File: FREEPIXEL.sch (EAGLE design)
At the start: 4 parts

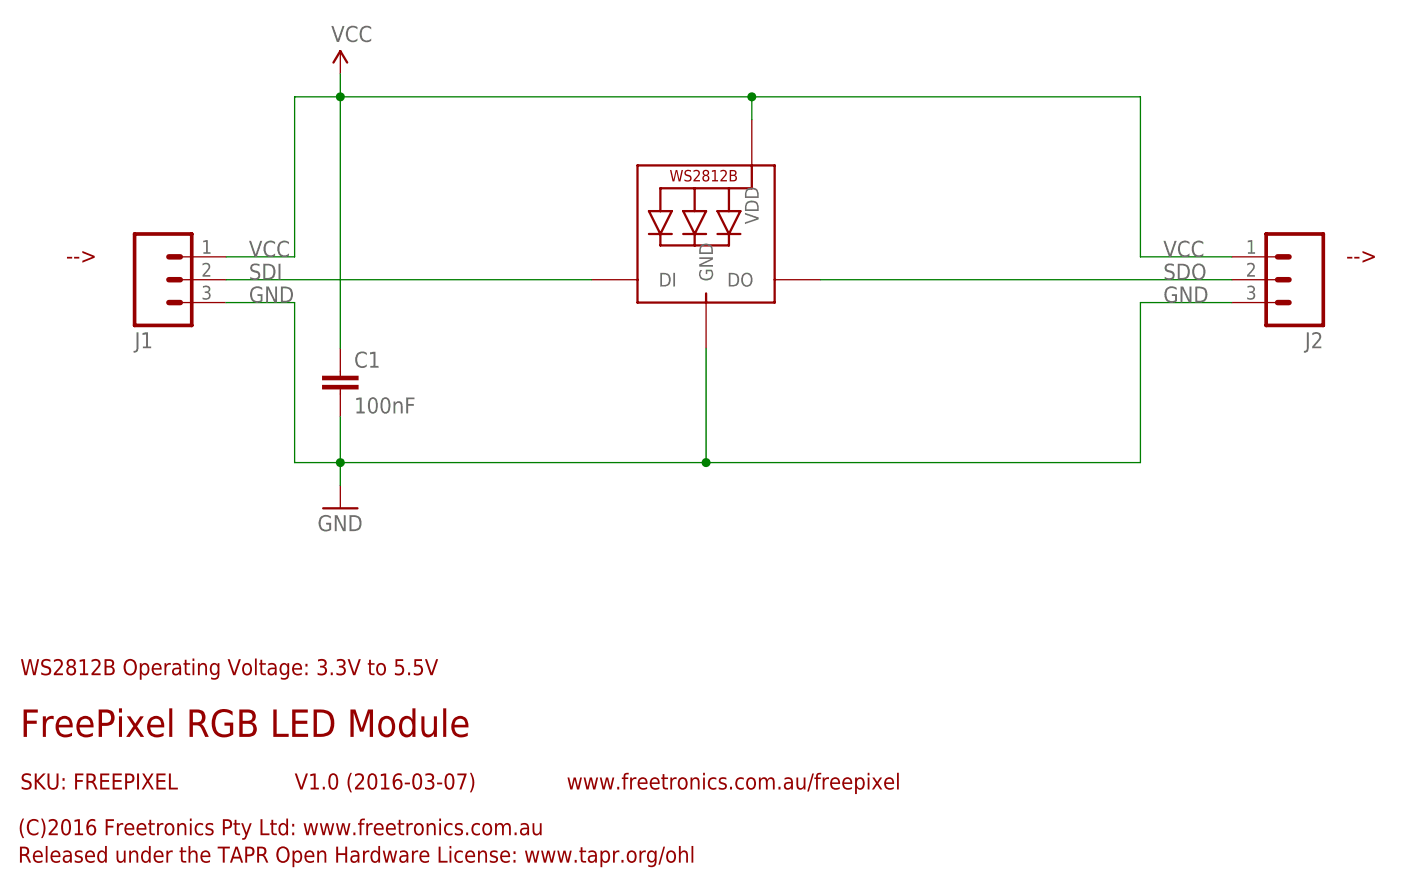
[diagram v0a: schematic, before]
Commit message: Clarified schematic
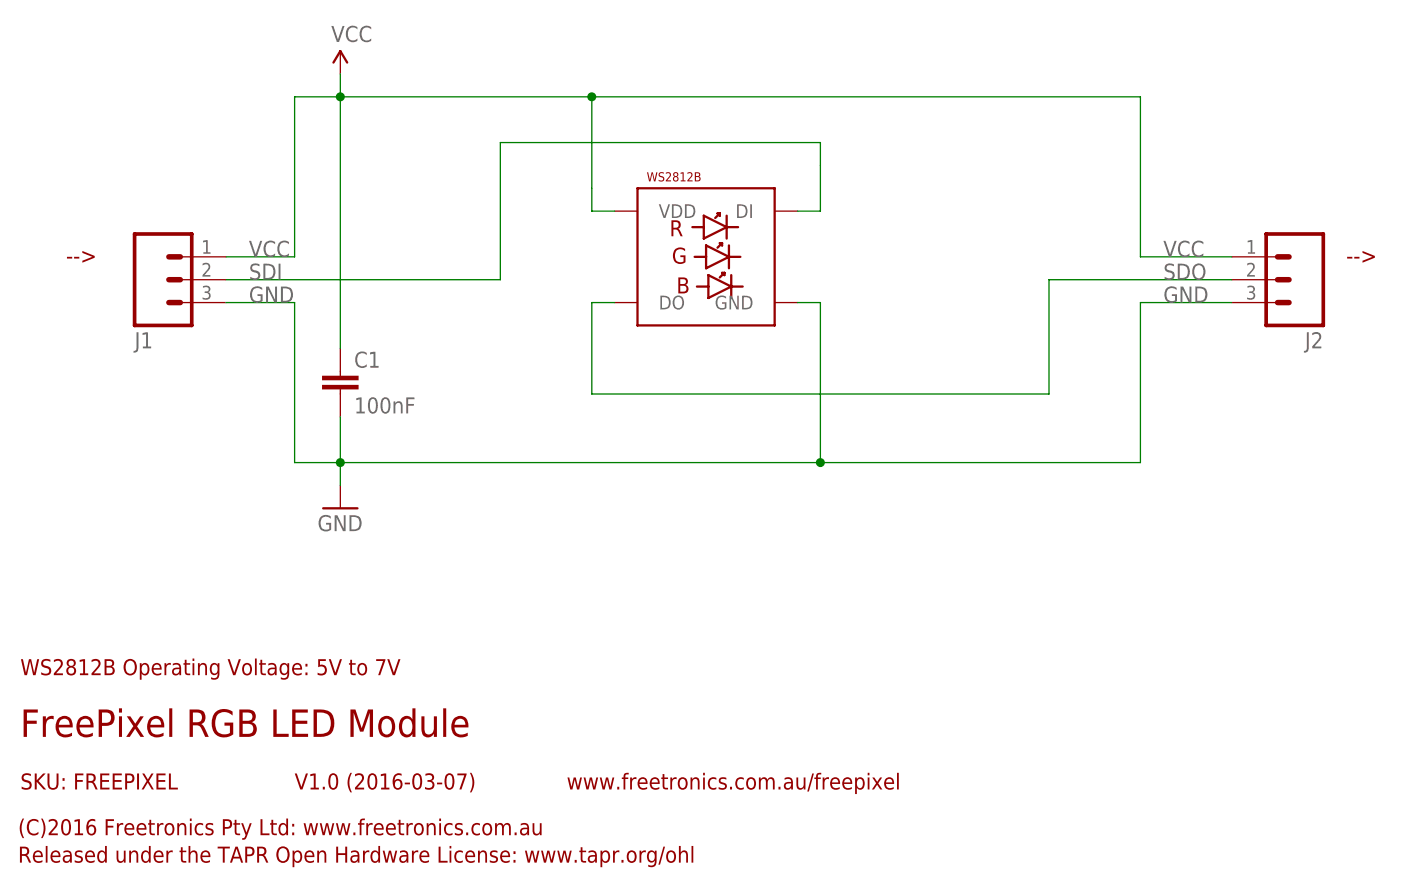
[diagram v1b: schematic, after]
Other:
- note added: "WS2812B Operating Voltage: 5V to 7V"
- note removed: "WS2812B Operating Voltage: 3.3V to 5.5V"
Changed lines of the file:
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@@
 <text x="7.366" y="6.35" size="1.778" layer="94">Released under the TAPR Open Hardware License: www.tapr.org/ohl</text>
 <text x="68.326" y="14.478" size="1.778" layer="94">www.freetronics.com.au/freepixel</text>
-<text x="7.62" y="27.178" size="1.778" layer="94">WS2812B Operating Voltage: 3.3V to 5.5V</text>
+<text x="7.62" y="27.178" size="1.778" layer="94">WS2812B Operating Voltage: 5V to 7V</text>
 <text x="12.7" y="72.898" size="1.778" layer="94">--&gt;</text>
 <text x="154.94" y="72.898" size="1.778" layer="94">--&gt;</text>
@@
 <pinref part="GND5" gate="1" pin="GND"/>
 <pinref part="J1" gate="G$1" pin="3"/>
-<wire x1="43.18" y1="50.8" x2="83.82" y2="50.8" width="0.1524" layer="91"/>
-<wire x1="83.82" y1="50.8" x2="132.08" y2="50.8" width="0.1524" layer="91"/>
+<wire x1="43.18" y1="50.8" x2="96.52" y2="50.8" width="0.1524" layer="91"/>
+<wire x1="96.52" y1="50.8" x2="132.08" y2="50.8" width="0.1524" layer="91"/>
 <wire x1="142.24" y1="68.58" x2="132.08" y2="68.58" width="0.1524" layer="91"/>
 <wire x1="132.08" y1="68.58" x2="132.08" y2="50.8" width="0.1524" layer="91"/>
@@
 <pinref part="J2" gate="G$1" pin="3"/>
 <pinref part="LED1" gate="G$1" pin="GND"/>
-<wire x1="83.82" y1="63.5" x2="83.82" y2="50.8" width="0.1524" layer="91"/>
-<junction x="83.82" y="50.8"/>
+<wire x1="93.98" y1="68.58" x2="96.52" y2="68.58" width="0.1524" layer="91"/>
+<wire x1="96.52" y1="68.58" x2="96.52" y2="50.8" width="0.1524" layer="91"/>
+<junction x="96.52" y="50.8"/>
 </segment>
 </net>
 <net name="SDI" class="0">
 <segment>
-<wire x1="30.48" y1="71.12" x2="71.12" y2="71.12" width="0.1524" layer="91"/>
+<wire x1="30.48" y1="71.12" x2="60.96" y2="71.12" width="0.1524" layer="91"/>
+<wire x1="60.96" y1="71.12" x2="60.96" y2="86.36" width="0.1524" layer="91"/>
+<wire x1="60.96" y1="86.36" x2="96.52" y2="86.36" width="0.1524" layer="91"/>
+<wire x1="96.52" y1="86.36" x2="96.52" y2="83.82" width="0.1524" layer="91"/>
+<wire x1="96.52" y1="83.82" x2="96.52" y2="78.74" width="0.1524" layer="91"/>
+<wire x1="96.52" y1="78.74" x2="93.98" y2="78.74" width="0.1524" layer="91"/>
 <label x="33.02" y="71.12" size="1.778" layer="95"/>
 <pinref part="LED1" gate="G$1" pin="DI"/>
@@
 <net name="SDO" class="0">
 <segment>
-<wire x1="96.52" y1="71.12" x2="142.24" y2="71.12" width="0.1524" layer="91"/>
+<wire x1="73.66" y1="68.58" x2="71.12" y2="68.58" width="0.1524" layer="91"/>
+<wire x1="71.12" y1="68.58" x2="71.12" y2="58.42" width="0.1524" layer="91"/>
+<wire x1="71.12" y1="58.42" x2="121.92" y2="58.42" width="0.1524" layer="91"/>
+<wire x1="121.92" y1="58.42" x2="121.92" y2="71.12" width="0.1524" layer="91"/>
+<wire x1="121.92" y1="71.12" x2="142.24" y2="71.12" width="0.1524" layer="91"/>
 <label x="134.62" y="71.12" size="1.778" layer="95"/>
 <pinref part="LED1" gate="G$1" pin="DO"/>
@@
 <label x="134.62" y="73.66" size="1.778" layer="95"/>
 <pinref part="J2" gate="G$1" pin="1"/>
-<wire x1="43.18" y1="91.44" x2="88.9" y2="91.44" width="0.1524" layer="91"/>
+<wire x1="43.18" y1="91.44" x2="71.12" y2="91.44" width="0.1524" layer="91"/>
 <pinref part="LED1" gate="G$1" pin="VDD"/>
-<wire x1="88.9" y1="91.44" x2="132.08" y2="91.44" width="0.1524" layer="91"/>
-<wire x1="88.9" y1="91.44" x2="88.9" y2="88.9" width="0.1524" layer="91"/>
-<junction x="88.9" y="91.44"/>
+<wire x1="71.12" y1="91.44" x2="132.08" y2="91.44" width="0.1524" layer="91"/>
+<wire x1="71.12" y1="91.44" x2="71.12" y2="81.28" width="0.1524" layer="91"/>
+<wire x1="71.12" y1="81.28" x2="71.12" y2="78.74" width="0.1524" layer="91"/>
+<wire x1="71.12" y1="78.74" x2="73.66" y2="78.74" width="0.1524" layer="91"/>
+<junction x="71.12" y="91.44"/>
 </segment>
 </net>

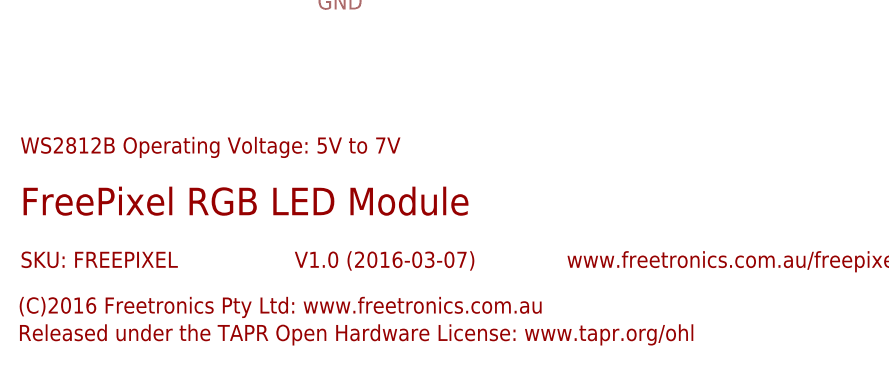
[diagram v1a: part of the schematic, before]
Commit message: Fixed silkscreen label for DI (Data In) on bottom for v1.1 release
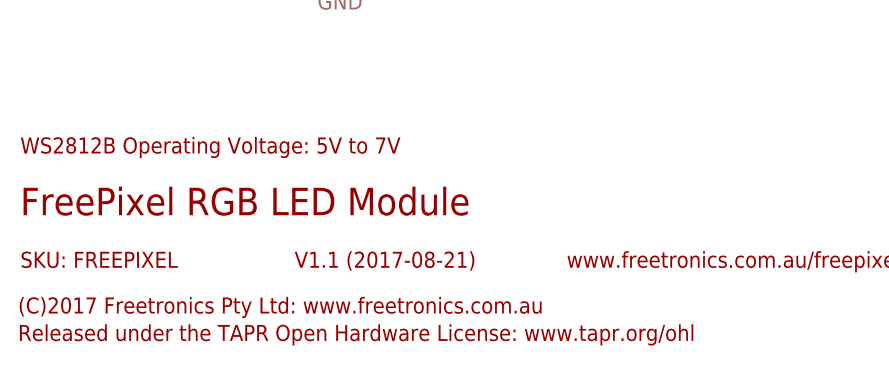
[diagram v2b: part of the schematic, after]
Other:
- note added: "(C)2017 Freetronics Pty Ltd: www.freetronics.com.au"
- note added: "V1.1 (2017-08-21)"
- note removed: "(C)2016 Freetronics Pty Ltd: www.freetronics.com.au"
- note removed: "V1.0 (2016-03-07)"
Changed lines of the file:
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@@
 <?xml version="1.0" encoding="utf-8"?>
 <!DOCTYPE eagle SYSTEM "eagle.dtd">
-<eagle version="6.5.0">
+<eagle version="8.2.2">
 <drawing>
 <settings>
@@
 <plain>
 <text x="7.62" y="20.32" size="3.048" layer="94">FreePixel RGB LED Module</text>
-<text x="38.1" y="14.478" size="1.778" layer="94">V1.0 (2016-03-07)</text>
+<text x="38.1" y="14.478" size="1.778" layer="94">V1.1 (2017-08-21)</text>
 <text x="7.62" y="14.478" size="1.778" layer="94">SKU: FREEPIXEL</text>
-<text x="7.366" y="9.398" size="1.778" layer="94">(C)2016 Freetronics Pty Ltd: www.freetronics.com.au</text>
+<text x="7.366" y="9.398" size="1.778" layer="94">(C)2017 Freetronics Pty Ltd: www.freetronics.com.au</text>
 <text x="7.366" y="6.35" size="1.778" layer="94">Released under the TAPR Open Hardware License: www.tapr.org/ohl</text>
 <text x="68.326" y="14.478" size="1.778" layer="94">www.freetronics.com.au/freepixel</text>
